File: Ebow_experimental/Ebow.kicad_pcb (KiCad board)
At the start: 2 copper layers, 69.8 x 30.5 mm, 10 parts, among them J1 Conn_01x02, U1 LM386

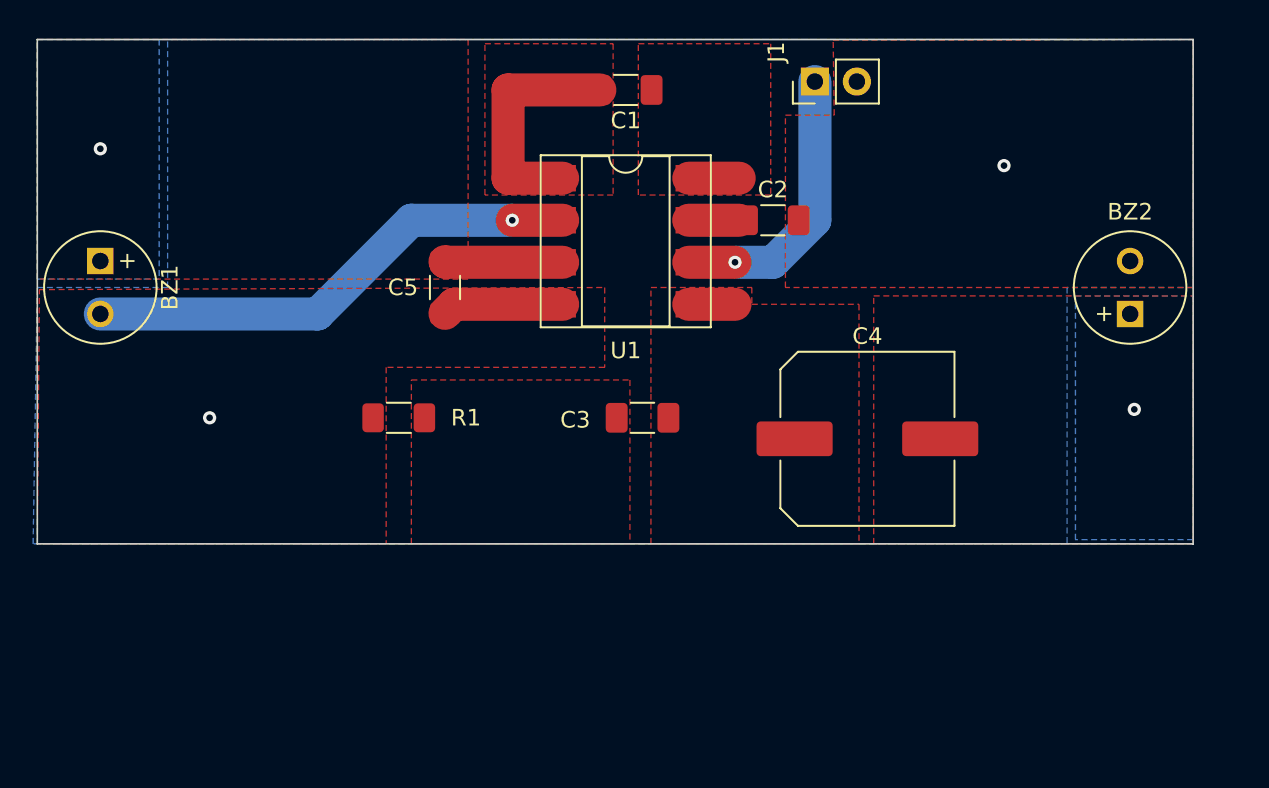
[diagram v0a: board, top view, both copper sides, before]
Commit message: Reconfigured as THT
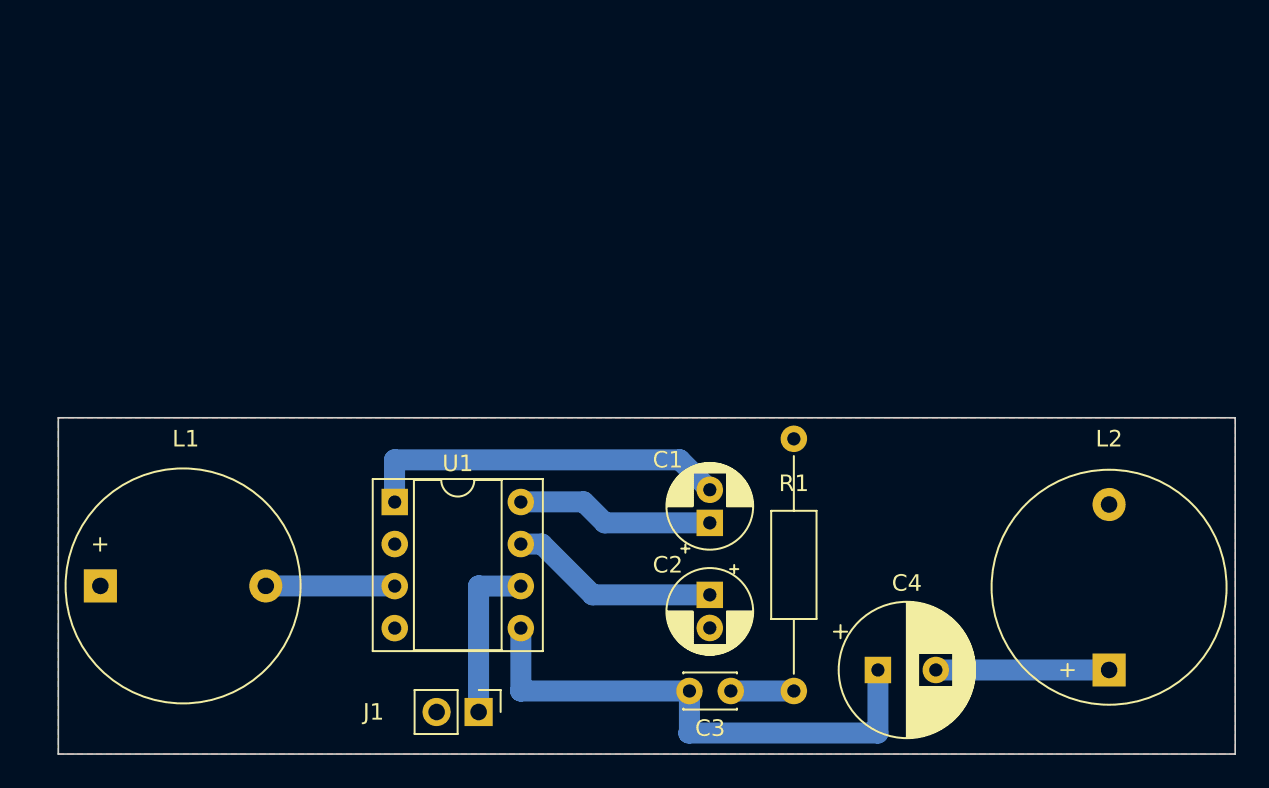
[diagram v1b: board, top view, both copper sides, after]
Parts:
- removed BZ1, BZ2: Buzzer, Buzzer_Beeper:MagneticBuzzer_Kingstate_KCG0601
- removed C5: 1nF, Capacitor_SMD:C_1206_3216Metric_Pad1.33x1.80mm_HandSolder
- added L1: L_Iron, Buzzer_Beeper:Buzzer_D14mm_H7mm_P10mm, F.Cu at (105.4, 83.8)
- added L2: L_Iron, Buzzer_Beeper:Buzzer_D14mm_H7mm_P10mm, F.Cu at (166.4, 88.9)
- C1, C2: footprint Capacitor_SMD:C_1206_3216Metric_Pad1.33x1.80mm_HandSolder -> Capacitor_THT:CP_Radial_D5.0mm_P2.00mm
- C3: footprint Capacitor_SMD:C_1206_3216Metric_Pad1.33x1.80mm_HandSolder -> Capacitor_THT:C_Disc_D3.0mm_W2.0mm_P2.50mm
- C4: footprint Capacitor_SMD:C_Elec_10x10.2 -> Capacitor_THT:CP_Radial_D8.0mm_P3.50mm
- R1: footprint Resistor_SMD:R_1206_3216Metric_Pad1.30x1.75mm_HandSolder -> Resistor_THT:R_Axial_DIN0207_L6.3mm_D2.5mm_P15.24mm_Horizontal
- U1: footprint Package_DIP:DIP-8_W7.62mm_SMDSocket_SmallPads -> Package_DIP:DIP-8_W7.62mm_Socket
- moved J1 43.2 mm to (128.3, 91.4), turned to -90 degrees
- moved R1 29.0 mm to (147.3, 90.2), turned to 90 degrees
- moved C1 26.7 mm to (142.2, 80.0), turned to 90 degrees
- moved C2 23.0 mm to (142.2, 84.4), turned to -90 degrees
- moved U1 21.1 mm to (123.2, 78.8)
- moved C3 17.4 mm to (143.5, 90.2), turned to 180 degrees
- moved C4 14.0 mm to (152.4, 88.9)
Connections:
- net Net-(C1-Pad1) renamed /GAIN2
- net Net-(C1-Pad2) renamed /GAIN1
- net Net-(C2-Pad1) renamed /BYPASS1
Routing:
- net GND: track 37.6 -> 0.00 mm, vias 3 -> 0
- net Net-(C3-Pad2): track 2.79 -> 31.8 mm
- net Net-(C4-Pad2): track 0.00 -> 10.5 mm, vias 1 -> 0
- net /BYPASS1: track 3.05 -> 12.7 mm
- net /GAIN2: track 3.05 -> 12.0 mm
- net /GAIN1: track 14.2 -> 22.3 mm
- net +5V: track 17.1 -> 10.2 mm, vias 1 -> 0
- net Net-(C3-Pad1): track 0.00 -> 3.81 mm
- net Net-(L1-Pad2): track 7.13 -> 7.78 mm, vias 1 -> 0
- removed copper zone on F.Cu, net /GAIN1
- removed copper zone on F.Cu, net /GAIN2
- removed copper zone on B.Cu, net GND
- removed copper zone on F.Cu, net Net-(C3-Pad1)
- removed copper zone on F.Cu, net Net-(C3-Pad2)
- removed copper zone on B.Cu, net Net-(C4-Pad2)
- removed copper zone on F.Cu, net Net-(C4-Pad2)
- removed copper zone on B.Cu, net Net-(L1-Pad2)
- removed copper zone on F.Cu, net Net-(L1-Pad2)
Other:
- board size 69.8 x 30.5 mm -> 71.1 x 20.3 mm
